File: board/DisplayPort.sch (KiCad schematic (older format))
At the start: 4 parts, among them J8 DISPLAY_PORT, J9 DISPLAY_PORT

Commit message: Issue #1683
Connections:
- net RXAUXCH_N renamed DPRXAUXCH_N
- net RXAUXCH_P renamed DPRXAUXCH_P
- net RXCONFIG1 renamed DPRXCONFIG1
- net RXCONFIG2 renamed DPRXCONFIG2
- net RX_HPD renamed DPRX_HPD
- net TXAUXCH_N renamed DPTXAUXCH_N
- net TXAUXCH_P renamed DPTXAUXCH_P
- net TXCONFIG1 renamed DPTXCONFIG1
- net TXCONFIG2 renamed DPTXCONFIG2
- net TX_HPD renamed DPTX_HPD
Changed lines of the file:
@@
 Sheet 6 12
 Title "HDMI2USB"
-Date "23 mar 2015"
+Date "25 mar 2015"
 Rev "Rev2"
 Comp ""
@@
 TX_LANEN3
 Text HLabel 3350 3250 0    60   BiDi ~ 0
-TXCONFIG1
+DPTXCONFIG1
 Text HLabel 3350 3350 0    60   BiDi ~ 0
-TXCONFIG2
+DPTXCONFIG2
 Text HLabel 7050 3300 0    60   BiDi ~ 0
-RXCONFIG1
+DPRXCONFIG1
 Text HLabel 7050 3400 0    60   BiDi ~ 0
-RXCONFIG2
+DPRXCONFIG2
 Text HLabel 3350 3450 0    60   BiDi ~ 0
-TXAUXCH_P
+DPTXAUXCH_P
 Text HLabel 3350 3650 0    60   BiDi ~ 0
-TXAUXCH_N
+DPTXAUXCH_N
 Text HLabel 7050 3500 0    60   BiDi ~ 0
-RXAUXCH_P
+DPRXAUXCH_P
 Text HLabel 7050 3700 0    60   BiDi ~ 0
-RXAUXCH_N
+DPRXAUXCH_N
 Text HLabel 3350 3750 0    60   BiDi ~ 0
-TX_HPD
+DPTX_HPD
 Text HLabel 7050 3800 0    60   BiDi ~ 0
-RX_HPD
+DPRX_HPD
 Text Label 6750 3900 0    39   ~ 0
 GND

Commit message: Issue #1670
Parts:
- added D3: DIODE, ~, symbol DIODE
- added R42, R45: 1M, ~, symbol R
- added R43, R46: 5M, ~, symbol R
- added R44, R47: 100K, ~, symbol R
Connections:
- net DPRXCONFIG1: now also R45.1
- net DPRXCONFIG2: now also R46.1
- net DPRX_HPD: now also R47.1
- net DPTXCONFIG1: now also R42.1
- net DPTXCONFIG2: now also R43.1
- net DPTX_HPD: now also R44.1
- net GND: now also R42.2, R43.2, R44.2, R45.2, R46.2, R47.2
- net at J8.20 (DP_PWR): now also D3.2 (K); no longer F3.2
- net RX_LANEN0 renamed DPRX_LANEN0
- net RX_LANEN1 renamed DPRX_LANEN1
- net RX_LANEN2 renamed DPRX_LANEN2
- net RX_LANEN3 renamed DPRX_LANEN3
- net RX_LANEP0 renamed DPRX_LANEP0
- net RX_LANEP1 renamed DPRX_LANEP1
- net RX_LANEP2 renamed DPRX_LANEP2
- net RX_LANEP3 renamed DPRX_LANEP3
- net TX_LANEN0 renamed DPTX_LANEN0
- net TX_LANEN1 renamed DPTX_LANEN1
- net TX_LANEN2 renamed DPTX_LANEN2
- net TX_LANEN3 renamed DPTX_LANEN3
- net TX_LANEP0 renamed DPTX_LANEP0
- net TX_LANEP1 renamed DPTX_LANEP1
- net TX_LANEP2 renamed DPTX_LANEP2
- net TX_LANEP3 renamed DPTX_LANEP3
- new net: D3.1 (A), F3.2
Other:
- note added: "DISPLAY PORT RX"
- note added: "DISPLAY PORT TX"
- moved on the sheet: F3
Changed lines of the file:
@@
 Sheet 6 12
 Title "HDMI2USB"
-Date "25 mar 2015"
+Date "30 mar 2015"
 Rev "Rev2"
 Comp ""
@@
 $EndComp
 Text Label 6700 2100 0    39   ~ 0
-RX_LANEP0
+DPRX_LANEP0
 Text Label 6700 2400 0    39   ~ 0
-RX_LANEP1
+DPRX_LANEP1
 Text Label 6700 2700 0    39   ~ 0
-RX_LANEP2
+DPRX_LANEP2
 Text Label 6700 3000 0    39   ~ 0
-RX_LANEP3
+DPRX_LANEP3
 Text Label 3000 2050 0    39   ~ 0
-TX_LANEP0
+DPTX_LANEP0
 Text Label 3000 2350 0    39   ~ 0
-TX_LANEP1
+DPTX_LANEP1
 Text Label 3000 2650 0    39   ~ 0
-TX_LANEP2
+DPTX_LANEP2
 Text Label 3000 2950 0    39   ~ 0
-TX_LANEP3
+DPTX_LANEP3
 Text Label 6700 2300 0    39   ~ 0
-RX_LANEN0
+DPRX_LANEN0
 Text Label 6700 2600 0    39   ~ 0
-RX_LANEN1
+DPRX_LANEN1
 Text Label 6700 2900 0    39   ~ 0
-RX_LANEN2
+DPRX_LANEN2
 Text Label 6700 3200 0    39   ~ 0
-RX_LANEN3
+DPRX_LANEN3
 Text Label 3000 2250 0    39   ~ 0
-TX_LANEN0
+DPTX_LANEN0
 Text Label 3000 2550 0    39   ~ 0
-TX_LANEN1
+DPTX_LANEN1
 Text Label 3000 2850 0    39   ~ 0
-TX_LANEN2
+DPTX_LANEN2
 Text Label 3000 3150 0    39   ~ 0
-TX_LANEN3
-Text HLabel 3350 3250 0    60   BiDi ~ 0
+DPTX_LANEN3
+Text HLabel 2000 3250 0    60   BiDi ~ 0
 DPTXCONFIG1
-Text HLabel 3350 3350 0    60   BiDi ~ 0
+Text HLabel 2000 3350 0    60   BiDi ~ 0
 DPTXCONFIG2
-Text HLabel 7050 3300 0    60   BiDi ~ 0
+Text HLabel 5450 3300 0    60   BiDi ~ 0
 DPRXCONFIG1
-Text HLabel 7050 3400 0    60   BiDi ~ 0
+Text HLabel 5450 3400 0    60   BiDi ~ 0
 DPRXCONFIG2
 Text HLabel 3350 3450 0    60   BiDi ~ 0
@@
 Text HLabel 7050 3700 0    60   BiDi ~ 0
 DPRXAUXCH_N
-Text HLabel 3350 3750 0    60   BiDi ~ 0
+Text HLabel 2900 3750 0    60   BiDi ~ 0
 DPTX_HPD
-Text HLabel 7050 3800 0    60   BiDi ~ 0
+Text HLabel 6400 3800 0    60   BiDi ~ 0
 DPRX_HPD
 Text Label 6750 3900 0    39   ~ 0
@@
 Wire Wire Line
 	7050 3900 6750 3900
-Text Label 3050 3850 0    39   ~ 0
-GND
-Wire Wire Line
-	3350 3850 3050 3850
-Text Label 2450 4150 0    39   ~ 0
+Text Label 3200 3850 0    39   ~ 0
+GND
+Text Label 4850 4450 2    39   ~ 0
 VCC3V3
 Wire Wire Line
-	2450 4150 2750 4150
+	4850 4450 4550 4450
 Wire Wire Line
 	3350 2050 3000 2050
@@
 Text Label 3050 3550 0    39   ~ 0
 GND
-Text GLabel 2450 4150 0    39   Input ~ 0
+Text GLabel 4850 4450 2    39   Input ~ 0
 VCC3V3
-Text GLabel 3050 3850 0    39   Input ~ 0
-GND
-Text HLabel 6400 1800 0    39   Input ~ 0
-RX_LANEP[0..3]
-Text HLabel 6400 1700 0    39   Input ~ 0
-RX_LANEN[0..3]
-Text HLabel 2700 1750 0    39   Output ~ 0
-TX_LANEP[0..3]
-Text HLabel 2700 1650 0    39   Output ~ 0
-TX_LANEN[0..3]
+Text GLabel 3200 3850 0    39   Input ~ 0
+GND
+Text HLabel 6400 1800 0    39   BiDi ~ 0
+DPRX_LANEP[0..3]
+Text HLabel 6400 1700 0    39   BiDi ~ 0
+DPRX_LANEN[0..3]
+Text HLabel 2700 1750 0    39   BiDi ~ 0
+DPTX_LANEP[0..3]
+Text HLabel 2700 1650 0    39   BiDi ~ 0
+DPTX_LANEN[0..3]
 Entry Wire Line
 	2900 3050 3000 3150
@@
 L FUSE F3
 U 1 1 54A97564
-P 3000 4150
-F 0 "F3" H 3100 4200 40  0000 C CNN
-F 1 "FUSE" H 2900 4100 40  0000 C CNN
-F 2 "~" H 3000 4150 60  0000 C CNN
-F 3 "~" H 3000 4150 60  0000 C CNN
-	1    3000 4150
-	1    0    0    -1
-$EndComp
-Text Notes 2850 4350 0    60   ~ 0
+P 4300 4450
+F 0 "F3" H 4400 4500 40  0000 C CNN
+F 1 "FUSE" H 4200 4400 40  0000 C CNN
+F 2 "~" H 4300 4450 60  0000 C CNN
+F 3 "~" H 4300 4450 60  0000 C CNN
+	1    4300 4450
+	-1   0    0    -1
+$EndComp
+Text Notes 4200 4350 0    60   ~ 0
 350mA
 Wire Wire Line
-	3250 4150 3300 4150
-Wire Wire Line
-	3300 4150 3300 3950
-Wire Wire Line
 	3300 3950 3350 3950
 Wire Wire Line
-	6900 4600 7100 4600
+	6500 4600 7100 4600
+Wire Wire Line
+	5450 3300 7050 3300
+Wire Wire Line
+	5450 3400 7050 3400
+Wire Wire Line
+	2000 3250 3350 3250
+Wire Wire Line
+	3350 3350 2000 3350
+$Comp
+L R R42
+U 1 1 551B13E6
+P 2100 3700
+F 0 "R42" V 2180 3700 40  0000 C CNN
+F 1 "1M" V 2107 3701 40  0000 C CNN
+F 2 "~" V 2030 3700 30  0000 C CNN
+F 3 "~" H 2100 3700 30  0000 C CNN
+	1    2100 3700
+	1    0    0    -1
+$EndComp
+$Comp
+L R R43
+U 1 1 551B13EC
+P 2250 3700
+F 0 "R43" V 2330 3700 40  0000 C CNN
+F 1 "5M" V 2257 3701 40  0000 C CNN
+F 2 "~" V 2180 3700 30  0000 C CNN
+F 3 "~" H 2250 3700 30  0000 C CNN
+	1    2250 3700
+	1    0    0    -1
+$EndComp
+Wire Wire Line
+	2100 3450 2100 3250
+Connection ~ 2100 3250
+Wire Wire Line
+	2250 3450 2250 3350
+Connection ~ 2250 3350
+Wire Wire Line
+	1850 3950 2250 3950
+Connection ~ 2100 3950
+Text Label 1850 3950 0    39   ~ 0
+GND
+$Comp
+L R R45
+U 1 1 551B14BF
+P 5550 3800
+F 0 "R45" V 5630 3800 40  0000 C CNN
+F 1 "1M" V 5557 3801 40  0000 C CNN
+F 2 "~" V 5480 3800 30  0000 C CNN
+F 3 "~" H 5550 3800 30  0000 C CNN
+	1    5550 3800
+	1    0    0    -1
+$EndComp
+$Comp
+L R R46
+U 1 1 551B14C5
+P 5700 3800
+F 0 "R46" V 5780 3800 40  0000 C CNN
+F 1 "5M" V 5707 3801 40  0000 C CNN
+F 2 "~" V 5630 3800 30  0000 C CNN
+F 3 "~" H 5700 3800 30  0000 C CNN
+	1    5700 3800
+	1    0    0    -1
+$EndComp
+Wire Wire Line
+	5550 3550 5550 3300
+Connection ~ 5550 3300
+Wire Wire Line
+	5700 3550 5700 3400
+Connection ~ 5700 3400
+Wire Wire Line
+	5300 4050 5700 4050
+Connection ~ 5550 4050
+Text Label 5300 4050 0    39   ~ 0
+GND
+Wire Wire Line
+	6400 3800 7050 3800
+$Comp
+L R R47
+U 1 1 551B307E
+P 6500 4350
+F 0 "R47" V 6580 4350 40  0000 C CNN
+F 1 "100K" V 6507 4351 40  0000 C CNN
+F 2 "~" V 6430 4350 30  0000 C CNN
+F 3 "~" H 6500 4350 30  0000 C CNN
+	1    6500 4350
+	1    0    0    -1
+$EndComp
+Wire Wire Line
+	6500 4100 6500 3800
+Connection ~ 6500 3800
+Connection ~ 6900 4600
+$Comp
+L R R44
+U 1 1 551B3100
+P 3000 4200
+F 0 "R44" V 3080 4200 40  0000 C CNN
+F 1 "100K" V 3007 4201 40  0000 C CNN
+F 2 "~" V 2930 4200 30  0000 C CNN
+F 3 "~" H 3000 4200 30  0000 C CNN
+	1    3000 4200
+	1    0    0    -1
+$EndComp
+Wire Wire Line
+	2900 3750 3350 3750
+Wire Wire Line
+	3300 3950 3300 4450
+Wire Wire Line
+	3300 4450 3650 4450
+Wire Wire Line
+	3200 3850 3350 3850
+Wire Wire Line
+	3000 3950 3000 3750
+Connection ~ 3000 3750
+Wire Wire Line
+	3000 4450 2800 4450
+Text Label 2800 4450 0    39   ~ 0
+GND
+$Comp
+L DIODE D3
+U 1 1 551C9BF5
+P 3850 4450
+F 0 "D3" H 3850 4550 40  0000 C CNN
+F 1 "DIODE" H 3850 4350 40  0000 C CNN
+F 2 "~" H 3850 4450 60  0000 C CNN
+F 3 "~" H 3850 4450 60  0000 C CNN
+	1    3850 4450
+	-1   0    0    1
+$EndComp
+Text Notes 3100 1450 0    118  ~ 24
+DISPLAY PORT TX
+Text Notes 6900 1500 0    118  ~ 24
+DISPLAY PORT RX
 $EndSCHEMATC

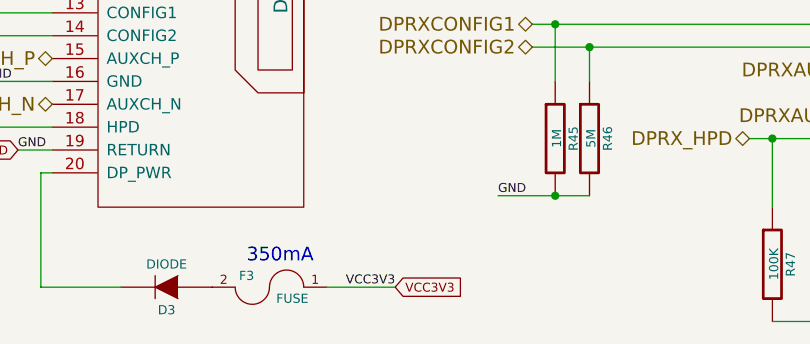
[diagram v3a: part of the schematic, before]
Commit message: Issue #1488 - Added diode display port power pin
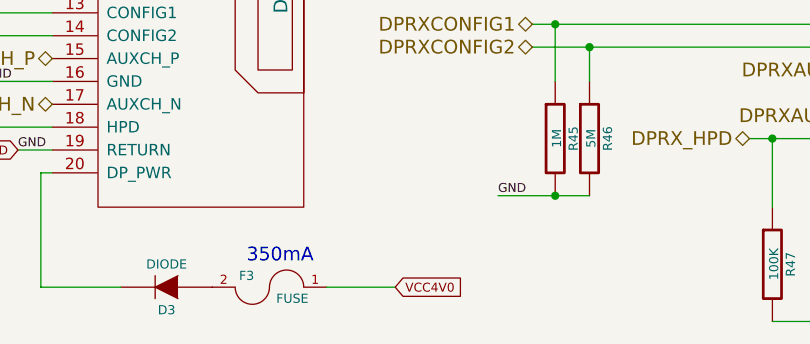
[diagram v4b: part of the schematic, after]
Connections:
- net VCC3V3 renamed VCC4V0
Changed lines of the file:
@@
 Text Label 3200 3850 0    39   ~ 0
 GND
-Text Label 4850 4450 2    39   ~ 0
-VCC3V3
 Wire Wire Line
 	4850 4450 4550 4450
@@
 GND
 Text GLabel 4850 4450 2    39   Input ~ 0
-VCC3V3
+VCC4V0
 Text GLabel 3200 3850 0    39   Input ~ 0
 GND

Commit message: Issue #1585
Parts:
- added D11: DIODE, ~, symbol DIODE
- added F2: FUSE, ~, symbol FUSE
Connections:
- net VCC4V0: now also F2.1
- net at J9.20 (DP_PWR), R25.1: now also D11.2 (K)
- new net: D11.1 (A), F2.2
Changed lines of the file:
@@
 LIBS:contrib
 LIBS:valves
-LIBS:hdmi2usb
-LIBS:timvideos-pcie-8x
 LIBS:HDMI2USB-cache
 EELAYER 27 0
@@
 Sheet 6 12
 Title "HDMI2USB"
-Date "30 mar 2015"
+Date "1 apr 2015"
 Rev "Rev2"
 Comp ""
@@
 Text Notes 6900 1500 0    118  ~ 24
 DISPLAY PORT RX
+Wire Wire Line
+	8850 4450 8550 4450
+Text GLabel 8850 4450 2    39   Input ~ 0
+VCC4V0
+$Comp
+L FUSE F2
+U 1 1 5523C11D
+P 8300 4450
+F 0 "F2" H 8400 4500 40  0000 C CNN
+F 1 "FUSE" H 8200 4400 40  0000 C CNN
+F 2 "~" H 8300 4450 60  0000 C CNN
+F 3 "~" H 8300 4450 60  0000 C CNN
+	1    8300 4450
+	-1   0    0    -1
+$EndComp
+Text Notes 8200 4350 0    60   ~ 0
+350mA
+Wire Wire Line
+	7100 4450 7650 4450
+$Comp
+L DIODE D11
+U 1 1 5523C125
+P 7850 4450
+F 0 "D11" H 7850 4550 40  0000 C CNN
+F 1 "DIODE" H 7850 4350 40  0000 C CNN
+F 2 "~" H 7850 4450 60  0000 C CNN
+F 3 "~" H 7850 4450 60  0000 C CNN
+	1    7850 4450
+	-1   0    0    1
+$EndComp
+Wire Wire Line
+	7100 4450 7100 4050
+Wire Wire Line
+	7100 4050 6900 4050
+Connection ~ 6900 4050
 $EndSCHEMATC

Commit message: Issue #1647 - Final changes
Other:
- note added: "500mA"
- note removed: "350mA"
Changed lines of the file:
@@
 LIBS:contrib
 LIBS:valves
+LIBS:hdmi2usb
+LIBS:timvideos-pcie-8x
 LIBS:HDMI2USB-cache
 EELAYER 27 0
@@
 Sheet 6 12
 Title "HDMI2USB"
-Date "1 apr 2015"
+Date "2 apr 2015"
 Rev "Rev2"
 Comp ""
@@
 	-1   0    0    -1
 $EndComp
-Text Notes 4200 4350 0    60   ~ 0
-350mA
 Wire Wire Line
 	3300 3950 3350 3950
@@
 $EndComp
 Text Notes 8200 4350 0    60   ~ 0
-350mA
+500mA
 Wire Wire Line
 	7100 4450 7650 4450
@@
 	7100 4050 6900 4050
 Connection ~ 6900 4050
+Text Notes 4150 4350 0    60   ~ 0
+500mA
 $EndSCHEMATC
